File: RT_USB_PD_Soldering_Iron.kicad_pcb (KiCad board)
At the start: 4 copper layers, 75 x 11 mm, 63 parts, among them J1 USB4105-GF-A, J2 35RASMT4BHNTRX, SW1 SW_Push, SW2 SW_Push, U1 SPX3819M5-L-3-3, U2 BMI270, U3 DRTR5V0U4S-7, U5 STM32G431Kxxx, U6 TPS25982ONRGET, U7 OPA376AIDCKR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

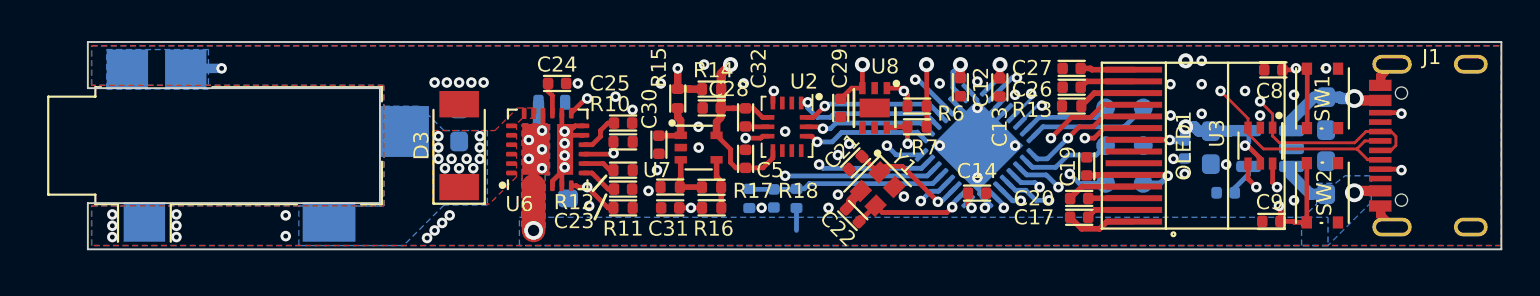
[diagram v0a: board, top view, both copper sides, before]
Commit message: Add castellated holes, improve connector cutout and pad placement
castellated holes to hopefully increase mechanical stability.
cut into corners
update schematic PDF.
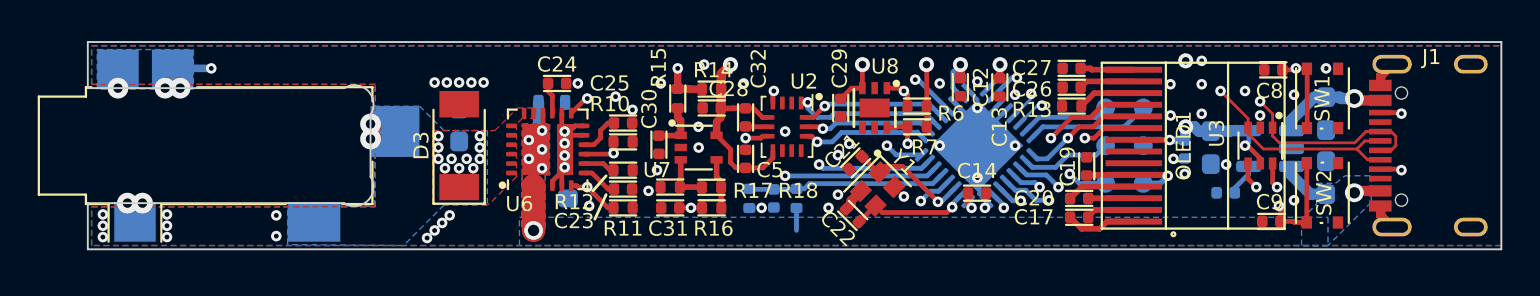
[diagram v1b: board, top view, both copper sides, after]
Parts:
- moved J2 0.50 mm to (103.5, 125.0)
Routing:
- net /BTN2: track 35.8 -> 21.2 mm
- net /TIP_TC: track 28.4 -> 28.3 mm, vias 2 -> 5
- net GND: vias 60 -> 62
- net /HEATER: vias 11 -> 13
- added copper zone on F.Cu, net /TIP_TC
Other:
- outline, holes or cut-outs redrawn

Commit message: remove test points and replace with connector. fix USB nets
also adjust default thermals for zone, sync pcb with schematic
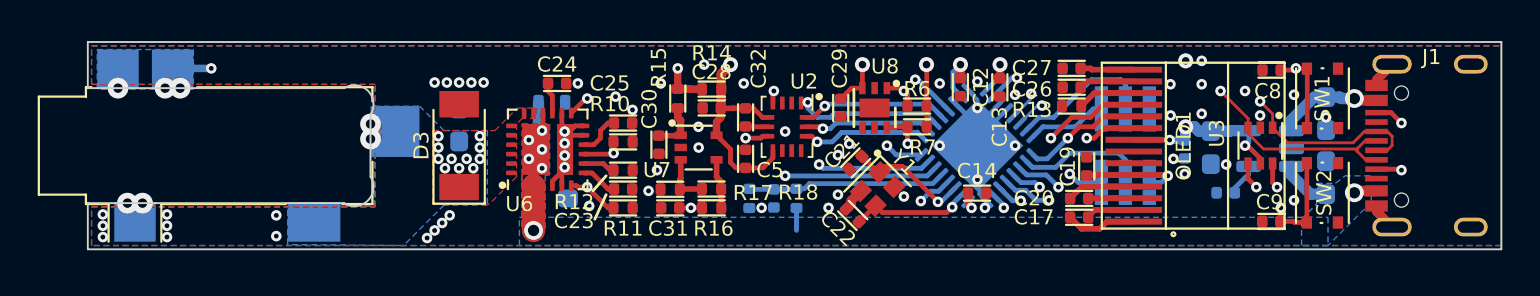
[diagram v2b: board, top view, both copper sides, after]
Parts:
- removed TP1, TP2, TP3, TP4, TP5, TP6: TestPoint, TestPoint:TestPoint_Pad_D1.0mm
- added J3: Conn_02x03_Odd_Even, Basic_SMD:PinHeader_2x03_P1.27mm_Vertical_SMD, B.Cu at (155.1, 125.0)
- R2: value 12K 1% -> 120K 1%
- R4: value 1.8K 1% -> 18K 1%
- moved R17 0.12 mm to (130.9, 127.3)
- moved R18 0.09 mm to (133.1, 127.3)
- moved C8 0.09 mm to (162.8, 121.0)
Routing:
- net /SWDIO: track 4.67 -> 7.75 mm
- net /SWCLK: track 6.47 -> 4.23 mm
- net /SWO: track 4.80 -> 7.02 mm

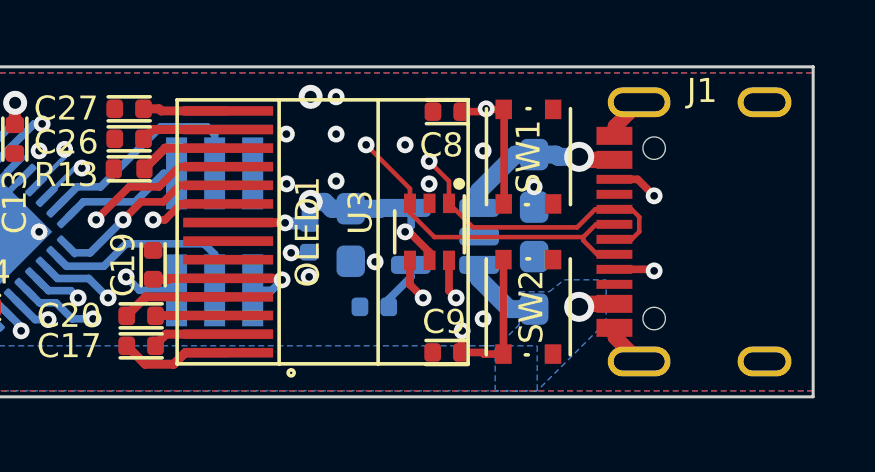
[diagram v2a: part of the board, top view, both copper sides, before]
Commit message: Update buttons to use active-high
by using active high, button1 allows boot mode selection when pressed.
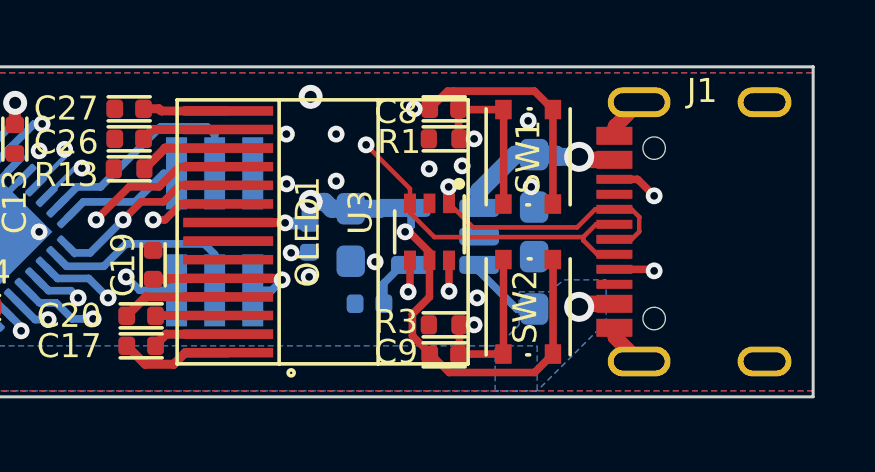
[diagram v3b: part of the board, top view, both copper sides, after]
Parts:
- added R1: 10K 5%, Basic_SMD:R_0402_1005Metric, F.Cu at (162.7, 121.9)
- added R3: 10K 5%, Basic_SMD:R_0402_1005Metric, F.Cu at (162.7, 128.1)
- moved C3 0.19 mm to (160.2, 127.4)
- moved C8 0.14 mm to (162.7, 120.9), turned to 0 degrees
- moved C9 0.12 mm to (162.7, 129.1), turned to 0 degrees
- turned SW1 to -90 degrees
- turned SW2 to -90 degrees
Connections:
- C8 pad 1: /BTN2 -> +3V3
- C8 pad 2: GND -> /BTN2
- C9 pad 1: /BTN1 -> +3V3
- C9 pad 2: GND -> /BTN1
- SW1 pad 1: /BTN2 -> +3V3
- SW1 pad 2: GND -> /BTN2
- SW2 pad 1: /BTN1 -> +3V3
- SW2 pad 2: GND -> /BTN1
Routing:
- net +3V3: track 75.8 -> 99.1 mm, vias 11 -> 12
- net /BTN1: track 21.1 -> 22.4 mm
- net /BTN2: track 21.3 -> 22.6 mm
- net /CC2: track 25.9 -> 24.7 mm
- net GND: vias 62 -> 61

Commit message: Group all used footprints in a local library
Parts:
- C1, C15, C16, C2, C33: footprint Capacitor_SMD:C_0603_1608Metric_Pad1.05x0.95mm_HandSolder -> local:C_0603_1608Metric_Pad1.05x0.95mm_HandSolder
- C12, C13, C14, C17, C18, C19, C20, C21, C22, C23, C24, C25, C26, C27, C28, C29, C3, C30, C31, C32, C4, C5, C8, C9: footprint Basic_SMD:C_0402_1005Metric -> local:C_0402_1005Metric
- D2: footprint D_1610:D_1610 -> local:D_1610
- D3: footprint Diode_SMD:D_SOD-128 -> local:D_SOD-128
- J1: footprint USB_C_GCT_USB4105:GCT_USB4105 -> local:GCT_USB4105
- J2: footprint 35RASMT4BHNTRX:Jack_3.5mm_CUI_SJ-3524-SMT_Horizontal_cutout -> local:Jack_3.5mm_CUI_SJ-3524-SMT_Horizontal_cutout
- J3: footprint Basic_SMD:PinHeader_2x03_P1.27mm_Vertical_SMD -> local:PinHeader_2x03_P1.27mm_Vertical_SMD
- OLED1: footprint ER-OLED0.87:ER-OLED0.87 -> local:ER-OLED0.87
- R1, R10, R11, R12, R13, R14, R15, R16, R17, R18, R2, R3, R4, R6, R7: footprint Basic_SMD:R_0402_1005Metric -> local:R_0402_1005Metric
- SW1, SW2: footprint Wurth:SW_Push_1P1T_NO_Vertical_Wuerth_434133025816 -> local:SW_Push_1P1T_NO_Vertical_Wuerth_434133025816
- U1: footprint Package_TO_SOT_SMD:SOT-23-5 -> local:SOT-23-5
- U2: footprint Package_LGA:Bosch_LGA-14_3x2.5mm_P0.5mm -> local:Bosch_LGA-14_3x2.5mm_P0.5mm
- U3: footprint Package_TO_SOT_SMD:SOT-363_SC-70-6 -> local:SOT-363_SC-70-6
- U5: footprint Package_DFN_QFN:QFN-32-1EP_5x5mm_P0.5mm_EP3.45x3.45mm -> local:QFN-32-1EP_5x5mm_P0.5mm_EP3.45x3.45mm
- U6: footprint TPS25982:VQFN-24-1EP_4x4mm_P0.5mm_EP2.45x2.45mm -> local:VQFN-24-1EP_4x4mm_P0.5mm_EP2.45x2.45mm
- U7: footprint Package_TO_SOT_SMD:SOT-353_SC-70-5 -> local:SOT-353_SC-70-5
- U8: footprint Package_DFN_QFN:DFN-6-1EP_2x2mm_P0.65mm_EP1x1.6mm -> local:DFN-6-1EP_2x2mm_P0.65mm_EP1x1.6mm
- Y1: footprint Crystal:Crystal_SMD_2016-4Pin_2.0x1.6mm -> local:Crystal_SMD_2016-4Pin_2.0x1.6mm

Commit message: Update Power voltage circuit to higher precision and lower cost components
change to 12K + 75K 0.5%
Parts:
- R2: value 120K 1% -> 75K 0.5%
- R4: value 18K 1% -> 12K 0.5%
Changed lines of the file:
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@@
     (property "Sheet file" "C:/Users/qwert/Documents/GitHub/Weller-RTx_USBC_PD_Iron/RT_USB_PD_Soldering_Iron.kicad_sch")
     (property "Sheet name" "")
-    (property "Tolerance" "1%")
+    (property "Tolerance" "0.5%")
     (attr smd)
     (fp_text reference "R4" (at -0.004522 1.1 -90) (layer "B.SilkS")
       (effects (font (size 0.8 0.8) (thickness 0.15)) (justify mirror))
     )
-    (fp_text value "18K 1%" (at 0 -1.17 -90) (layer "B.Fab")
+    (fp_text value "12K 0.5%" (at 0 -1.17 -90) (layer "B.Fab")
       (effects (font (size 1 1) (thickness 0.15)) (justify mirror))
     )
@@
     (property "Sheet file" "C:/Users/qwert/Documents/GitHub/Weller-RTx_USBC_PD_Iron/RT_USB_PD_Soldering_Iron.kicad_sch")
     (property "Sheet name" "")
-    (property "Tolerance" "1%")
+    (property "Tolerance" "0.5%")
     (attr smd)
     (fp_text reference "R2" (at 0 1.1 90) (layer "B.SilkS")
       (effects (font (size 0.8 0.8) (thickness 0.15)) (justify mirror))
     )
-    (fp_text value "120K 1%" (at 0 -1.17 90) (layer "B.Fab")
-      (effects (font (size 1 1) (thickness 0.15)) (justify mirror))
-    )
+    (fp_text value "75K 0.5%" (at 0 -1.17 90) (layer "B.Fab")
+      (effects (font (size 1 1) (thickness 0.15)) (justify mirror))
+    )

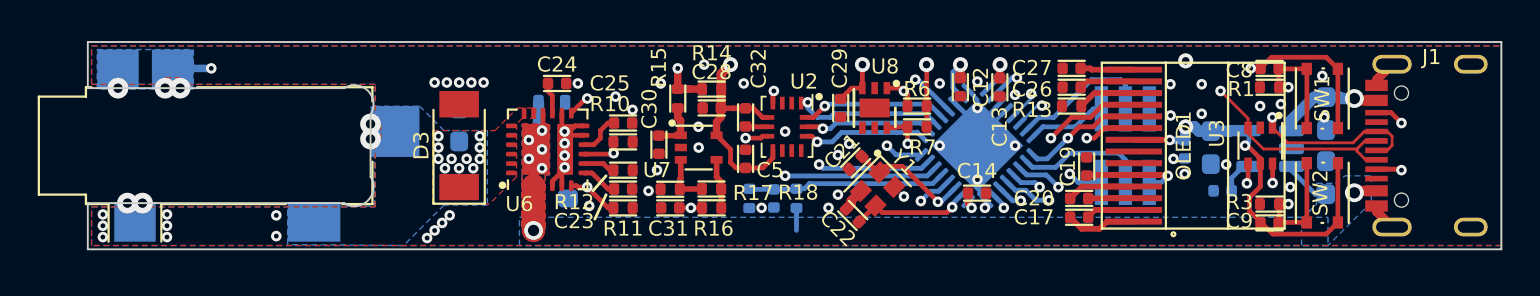
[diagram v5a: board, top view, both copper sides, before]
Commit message: update thermals for high side switch
or more accurately, add thermals. Previously difficult to hand solder. Hopefully this helps.
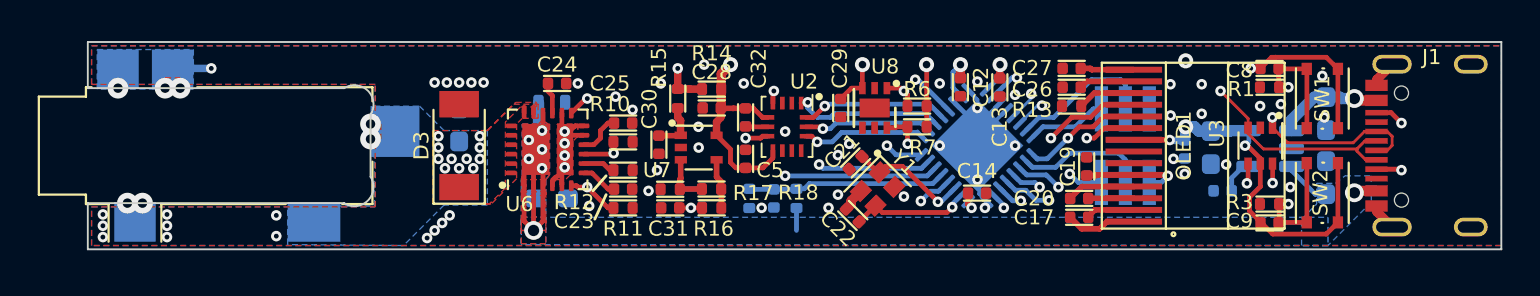
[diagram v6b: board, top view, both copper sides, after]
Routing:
- net IN: track 20.5 -> 31.9 mm
- net /HEATER: track 0.00 -> 0.65 mm
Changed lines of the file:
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@@
       (net 6 "/HEATER") (pinfunction "K"))
     (pad "2" smd rect (at 2.2 0 90) (size 1.4 2.1) (layers "F.Cu" "F.Paste" "F.Mask")
-      (net 25 "GND") (pinfunction "A"))
+      (net 25 "GND") (pinfunction "A") (zone_connect 1) (thermal_width 0.508))
     (model "${KISYS3DMOD}/Diode_SMD.3dshapes/D_SOD-128.wrl"
       (offset (xyz 0 0 0))
@@
       (net 6 "/HEATER") (pinfunction "OUT"))
     (pad "25" smd rect (at 0 -0.625 90) (size 2.7 1.45) (layers "F.Cu" "F.Mask")
-      (net 1 "IN") (pinfunction "IN"))
+      (net 1 "IN") (pinfunction "IN") (zone_connect 2))
     (pad "26" smd rect (at 0 0.925 90) (size 2.7 0.85) (layers "F.Cu" "F.Mask")
       (net 25 "GND") (pinfunction "GND"))
@@
   (gr_line (start 100 121.95) (end 100 119.5) (layer "Edge.Cuts") (width 0.1))
   (segment (start 167.3 122.6) (end 167.2 122.5) (width 0.55) (layer "F.Cu") (net 1))
+  (segment (start 124.15 127.125) (end 124.15 125.575) (width 0.254) (layer "F.Cu") (net 1))
+  (segment (start 123.65 125.325) (end 123.775 125.2) (width 0.254) (layer "F.Cu") (net 1))
+  (segment (start 123.65 127.125) (end 123.65 125.325) (width 0.254) (layer "F.Cu") (net 1))
+  (segment (start 123.15 125.825) (end 123.775 125.2) (width 0.254) (layer "F.Cu") (net 1))
+  (segment (start 123.15 127.125) (end 123.15 125.825) (width 0.254) (layer "F.Cu") (net 1))
   (segment (start 167.3 127.4) (end 167.2 127.5) (width 0.55) (layer "F.Cu") (net 1))
+  (segment (start 124.15 125.575) (end 123.775 125.2) (width 0.254) (layer "F.Cu") (net 1))
+  (segment (start 124.15 127.125) (end 124.15 129) (width 0.254) (layer "F.Cu") (net 1))
+  (segment (start 123.150001 129.000001) (end 123.65 129.5) (width 0.254) (layer "F.Cu") (net 1))
   (segment (start 168.4 127.4) (end 167.3 127.4) (width 0.55) (layer "F.Cu") (net 1))
+  (segment (start 123.15 127.125) (end 123.150001 129.000001) (width 0.254) (layer "F.Cu") (net 1))
   (segment (start 168.4 122.6) (end 167.3 122.6) (width 0.55) (layer "F.Cu") (net 1))
   (segment (start 124.15 123.275) (end 124.15 124.15) (width 0.254) (layer "F.Cu") (net 1))
-  (segment (start 123.65 127.125) (end 123.65 129.5) (width 1.25) (layer "F.Cu") (net 1))
+  (segment (start 123.65 127.125) (end 123.65 129.5) (width 0.254) (layer "F.Cu") (net 1))
+  (segment (start 124.15 129) (end 123.65 129.5) (width 0.254) (layer "F.Cu") (net 1))
   (via (at 123.4 124.7) (size 0.56) (drill 0.254) (layers "F.Cu" "B.Cu") (remove_unused_layers) (keep_end_layers) (net 1))
   (via (at 123.4 125.7) (size 0.56) (drill 0.254) (layers "F.Cu" "B.Cu") (remove_unused_layers) (keep_end_layers) (net 1))
@@
   (segment (start 148.039689 122.392544) (end 149.032233 121.4) (width 0.254) (layer "B.Cu") (net 5))
   (segment (start 149.032233 121.4) (end 149.3 121.4) (width 0.254) (layer "B.Cu") (net 5))
+  (segment (start 123.15 123.275) (end 123.15 122.95) (width 0.254) (layer "F.Cu") (net 6))
+  (segment (start 123.65 123.275) (end 123.65 122.95) (width 0.254) (layer "F.Cu") (net 6))
   (via (at 115 124.65) (size 1.1) (drill 0.5) (layers "F.Cu" "B.Cu") (remove_unused_layers) (keep_end_layers) (net 6))
   (via (at 118.6 125.7) (size 0.56) (drill 0.254) (layers "F.Cu" "B.Cu") (remove_unused_layers) (keep_end_layers) (net 6))
@@
   (segment (start 149.453903 123.806757) (end 150.38566 122.875) (width 0.1524) (layer "B.Cu") (net 54))
   (segment (start 150.38566 122.875) (end 150.625 122.875) (width 0.1524) (layer "B.Cu") (net 54))
+  (zone (net 1) (net_name "IN") (layer "F.Cu") (name "GND") (hatch edge 0.508)
+    (priority 1)
+    (connect_pads (clearance 0.1524))
+    (min_thickness 0.1524) (filled_areas_thickness no)
+    (fill yes (thermal_gap 0.1524) (thermal_bridge_width 0.508) (smoothing fillet) (radius 0.1))
+    (polygon
+      (pts
+        (xy 124.3 127.65)
+        (xy 123 127.65)
+        (xy 123 126.8)
+        (xy 124.3 126.8)
+      )
+    )
+  )
+  (zone (net 1) (net_name "IN") (layers F&B.Cu) (name "GND") (hatch edge 0.508)
+    (priority 1)
+    (connect_pads yes (clearance 0.1524))
+    (min_thickness 0.1524) (filled_areas_thickness no)
+    (fill yes (thermal_gap 0.1524) (thermal_bridge_width 0.508) (smoothing fillet) (radius 0.7))
+    (polygon
+      (pts
+        (xy 124.3 130.2)
+        (xy 123 130.2)
+        (xy 123 128.8)
+        (xy 124.3 128.8)
+      )
+    )
+  )
+  (zone (net 25) (net_name "GND") (layer "F.Cu") (name "GND") (hatch edge 0.508)
+    (priority 1)
+    (connect_pads yes (clearance 0.1524))
+    (min_thickness 0.1524) (filled_areas_thickness no)
+    (fill yes (thermal_gap 0.1524) (thermal_bridge_width 0.508) (smoothing fillet) (radius 0.7))
+    (polygon
+      (pts
+        (xy 126 124.5)
+        (xy 125.75 124.75)
+        (xy 125.75 126.55)
+        (xy 125.6 126.55)
+        (xy 125.05 127.1)
+        (xy 125.05 126.8)
+        (xy 124.55 126.8)
+        (xy 124.9 126.45)
+        (xy 124.9 123.85)
+        (xy 126 123.85)
+      )
+    )
+  )
   (zone (net 25) (net_name "GND") (layers "F.Cu" "In1.Cu" "In2.Cu" "B.Cu") (name "GND") (hatch edge 0.508)
     (connect_pads (clearance 0.1524))
@@
   (zone (net 6) (net_name "/HEATER") (layer "F.Cu") (name "GND") (hatch edge 0.508)
     (priority 1)
+    (connect_pads (clearance 0.1524))
+    (min_thickness 0.1524) (filled_areas_thickness no)
+    (fill yes (thermal_gap 0.1524) (thermal_bridge_width 0.508) (smoothing fillet) (radius 0.1))
+    (polygon
+      (pts
+        (xy 123.9 123.55)
+        (xy 123.05 123.55)
+        (xy 122.75 123.85)
+        (xy 122.75 126.75)
+        (xy 121.4 128.1)
+        (xy 121.1 128.1)
+        (xy 121.1 124.2)
+        (xy 121.2 124.2)
+        (xy 122.6 122.8)
+        (xy 123.9 122.8)
+      )
+    )
+  )
+  (zone (net 6) (net_name "/HEATER") (layer "F.Cu") (name "GND") (hatch edge 0.508)
+    (priority 1)
     (connect_pads yes (clearance 0.1524))
     (min_thickness 0.1524) (filled_areas_thickness no)
-    (fill yes (thermal_gap 0.2032) (thermal_bridge_width 0.508) (smoothing fillet) (radius 0.2))
+    (fill yes (thermal_gap 0.1524) (thermal_bridge_width 0.508) (smoothing fillet) (radius 0.2))
     (polygon
       (pts
-        (xy 123.775 123.55)
-        (xy 123.05 123.55)
-        (xy 122.75 123.85)
-        (xy 122.75 126.65)
+        (xy 123.8 122.95)
+        (xy 122.95 122.95)
+        (xy 122.15 123.75)
+        (xy 122.15 127.25)
         (xy 121.3 128.1)
         (xy 118.3 128.1)
         (xy 118.3 124.2)
-        (xy 121.6 124.2)
-        (xy 122.8 123)
-        (xy 123.775 123)
+        (xy 121.2 124.2)
+        (xy 122.7 122.7)
+        (xy 123.8 122.7)
       )
     )
   )
-  (zone (net 1) (net_name "IN") (layers F&B.Cu) (name "GND") (hatch edge 0.508)
+  (zone (net 1) (net_name "IN") (layer "F.Cu") (name "GND") (hatch edge 0.508)
     (priority 1)
     (connect_pads yes (clearance 0.1524))
     (min_thickness 0.1524) (filled_areas_thickness no)
-    (fill yes (thermal_gap 0.2032) (thermal_bridge_width 0.508) (smoothing fillet) (radius 0.1))
+    (fill yes (thermal_gap 0.1524) (thermal_bridge_width 0.508) (smoothing fillet) (radius 0.1))
+    (polygon
+      (pts
+        (xy 124.3 129.5)
+        (xy 123 129.5)
+        (xy 123 127.45)
+        (xy 124.3 127.45)
+      )
+    )
+  )
+  (zone (net 1) (net_name "IN") (layer "F.Cu") (name "GND") (hatch edge 0.508)
+    (priority 1)
+    (connect_pads yes (clearance 0.1524))
+    (min_thickness 0.1524) (filled_areas_thickness no)
+    (fill yes (thermal_gap 0.1524) (thermal_bridge_width 0.508) (smoothing fillet) (radius 0.1))
     (polygon
       (pts
         (xy 124.5 126.55)
-        (xy 124.275 126.55)
-        (xy 124.275 127.55)
-        (xy 124.275 129.3)
-        (xy 124.075 129.75)
-        (xy 123.65 129.925)
-        (xy 123.225 129.75)
-        (xy 123.025 129.3)
-        (xy 123.025 126.875)
+        (xy 124.3 126.8)
+        (xy 123 126.8)
         (xy 123.05 126.55)
         (xy 123.05 123.85)
+        (xy 123.9 123.85)
+        (xy 124 123.75)
+        (xy 124.3 123.75)
+        (xy 124.4 123.85)
         (xy 124.5 123.85)
       )
@@
       (pts
         (xy 165.8 130.3)
-        (xy 122.9 130.3)
-        (xy 122.9 128.8)
+        (xy 123 130.25)
+        (xy 123 128.8)
         (xy 165.8 128.8)
       )
@@
       )
     )
+  )
+  (zone (net 1) (net_name "IN") (layer "B.Cu") (name "GND") (hatch edge 0.508)
+    (priority 1)
+    (connect_pads yes (clearance 0.1524))
+    (min_thickness 0.1524) (filled_areas_thickness no)
+    (fill yes (thermal_gap 0.1524) (thermal_bridge_width 0.508) (smoothing fillet) (radius 0.1))
+    (polygon
+      (pts
+        (xy 124.3 129.5)
+        (xy 123 129.5)
+        (xy 123 126.8)
+        (xy 123.05 126.6)
+        (xy 123.05 123.85)
+        (xy 124.5 123.85)
+        (xy 124.5 126.55)
+        (xy 124.3 126.8)
+      )
+    )

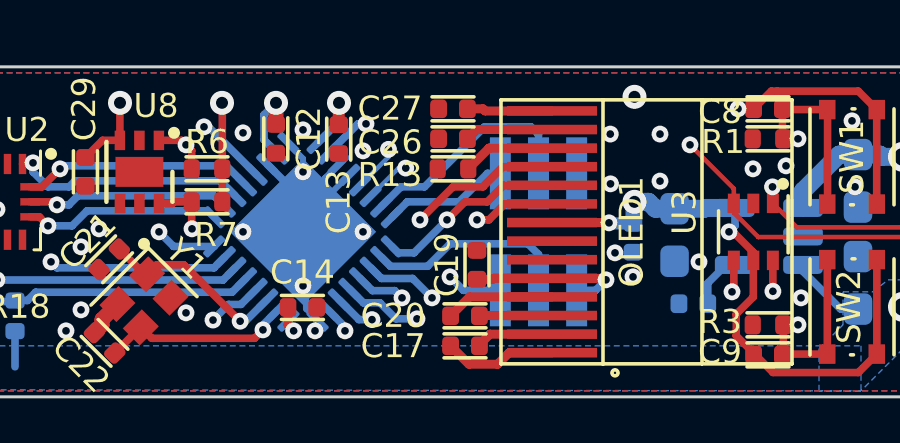
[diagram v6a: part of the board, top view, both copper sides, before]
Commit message: Update footprints for R26, R27
These 2.2uF capacitors are slightly larger than normal. Requires bigger pads.
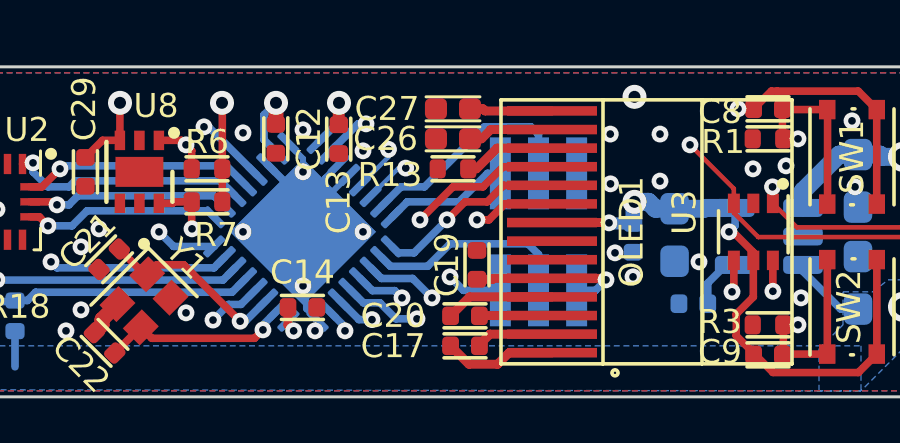
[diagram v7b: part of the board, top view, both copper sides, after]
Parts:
- C26, C27: footprint local:C_0402_1005Metric -> local:C_0402_1005Metric_Pad0.74x0.62mm_HandSolder
